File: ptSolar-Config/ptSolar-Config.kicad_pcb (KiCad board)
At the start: 2 copper layers, 17.4 x 53 mm, 12 parts, among them J1 6 Pin Male Header, J2 Programming, J3 USB_B_Micro, SW1 Reset Switch, U1 CH340X

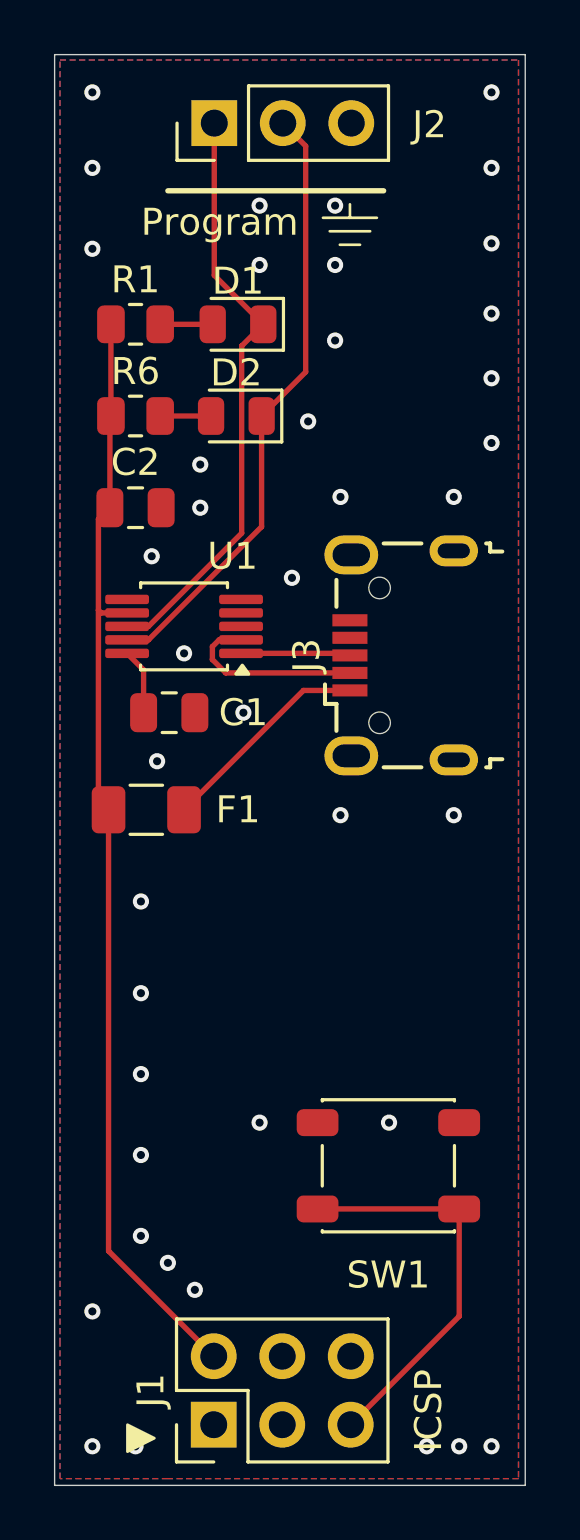
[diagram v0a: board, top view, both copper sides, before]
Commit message: Updated to firmware 1.0.1
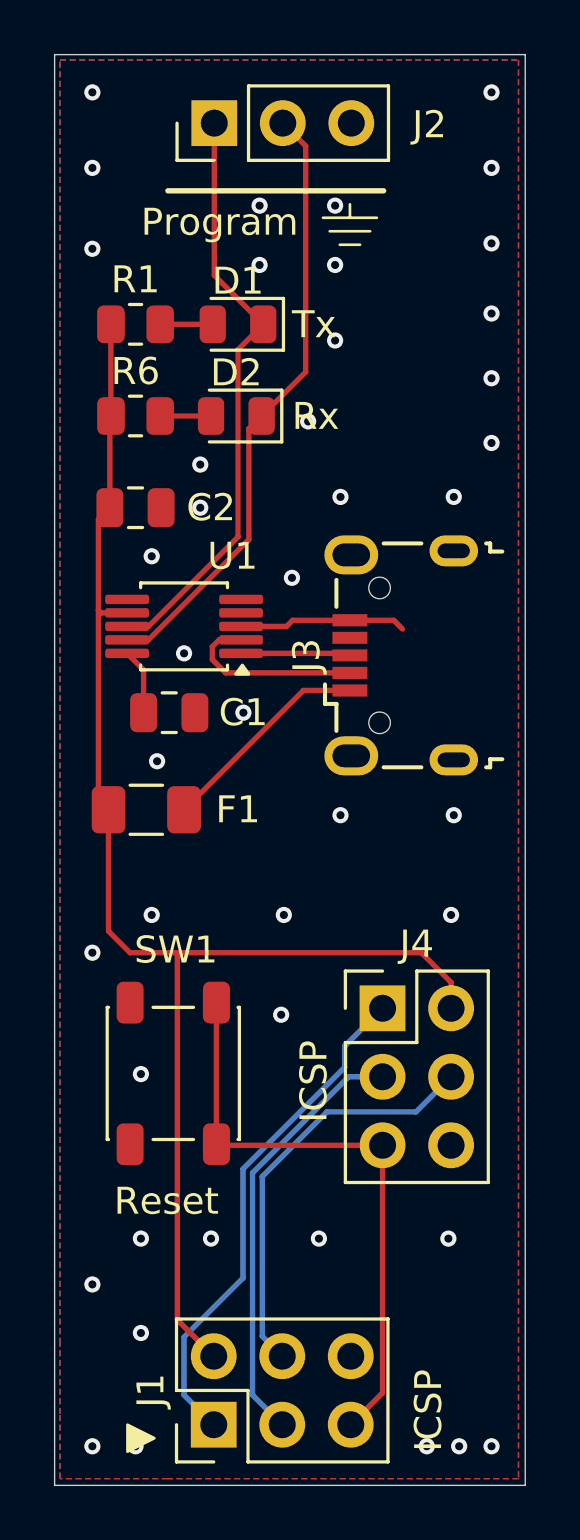
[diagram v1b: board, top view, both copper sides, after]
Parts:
- added J4: 6 Pin Male Header, Connector_PinHeader_2.54mm:PinHeader_2x03_P2.54mm_Vertical, F.Cu at (162.0, 123.6)
- moved SW1 8.68 mm to (154.2, 126.0), turned to -90 degrees
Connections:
- J1 pad 1: unconnected-(J1-Pin_1-Pad1) -> Net-(J1-Pin_1)
- J1 pad 3: unconnected-(J1-Pin_3-Pad3) -> Net-(J1-Pin_3)
- J1 pad 4: unconnected-(J1-Pin_4-Pad4) -> Net-(J1-Pin_4)
- U1 pad 3: unconnected-(U1-GND-Pad3) -> GND
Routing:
- net Net-(J1-Pin_1): track 0.00 -> 18.9 mm
- net Net-(J1-Pin_3): track 0.00 -> 16.1 mm
- net Net-(J1-Pin_4): track 0.00 -> 15.5 mm
- net +5V: track 41.3 -> 53.9 mm
- net Net-(J1-Pin_5): track 14.9 -> 22.3 mm
- net GND: track 0.00 -> 6.22 mm, vias 41 -> 43
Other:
- board text added: "Custom Digital Services, LLC ptSolar Config Cable v1.1.0"
- board text added: "Reset"
- board text added: "Rx"
- board text added: "Tx"
